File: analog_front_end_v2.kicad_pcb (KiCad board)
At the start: 4 copper layers, 153 parts, among them J1 Conn_Coaxial, J3 Conn_01x01_Socket, J4 Conn_01x01_Socket, U1 ADL5531, U10 PMOD 2x6, U11 LP2985-5.0, U12 LP2985-5.0, U13 LT1363, U14 MAX 735, U15 LP2985-2.5, U16 MAX889SESA, U17 MAX6102, U2 ADL5531, U3 ADL5531, U4 PE4140B-Z, U5 ADF4360-9, U6 LTC1406, U7 THS4551, U8 LT1363, U9 PMOD 2x6

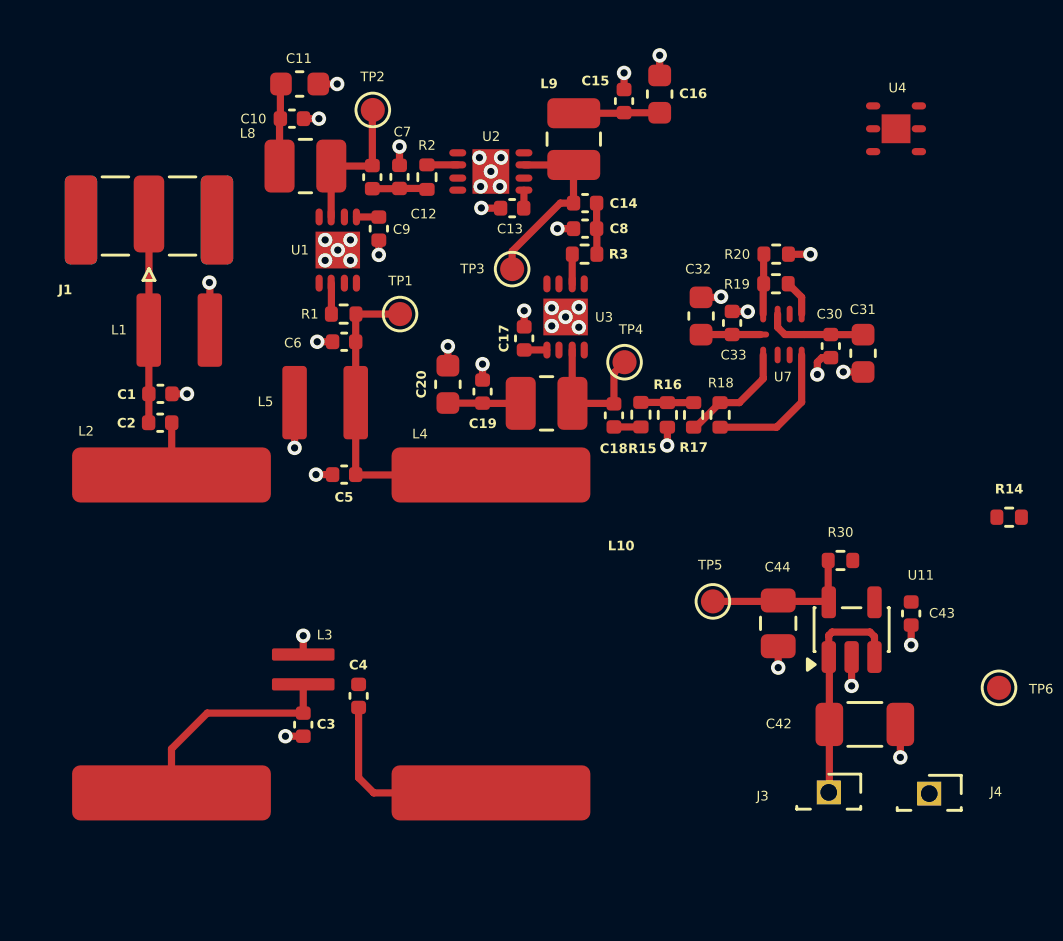
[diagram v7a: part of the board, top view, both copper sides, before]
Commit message: Minor touchups to via placements to bring them as close as possible to the pads for minimized parasitics
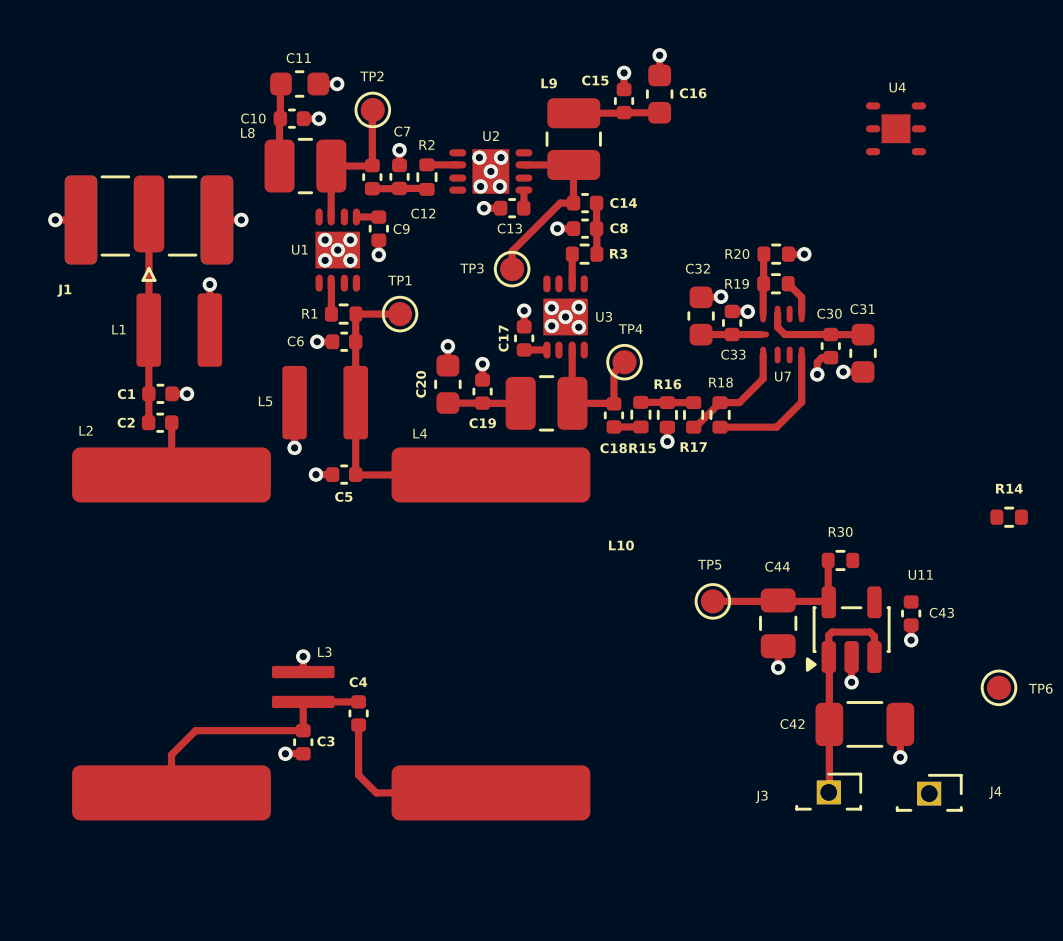
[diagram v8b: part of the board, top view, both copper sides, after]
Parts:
- moved C3 0.73 mm to (23.6, 42.0)
- moved C4 0.73 mm to (25.9, 40.8)
- moved L3 0.73 mm to (23.6, 39.7)
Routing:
- net Net-(C3-Pad1): track 9.12 -> 11.0 mm
- net GND: track 25.9 -> 27.0 mm, vias 44 -> 46
- net Net-(C4-Pad2): track 8.68 -> 7.89 mm
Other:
- board text added: "TODO: Ground via stitching Decisions: Use 0.3mm trace for 50ohm characteristic impedance for microstrip with solid groundplane in layers 2,3 Use 0.4mm silkscreen width/height to balance readability/placement Ensure RF Mixer (U4) is far away from sensitive RF/analog front end"
- board text removed: "TODO: Ground via stitching Decisions: Use 0.3mm trace for 50ohm characteristic impedance for microstrip with solid groundplane Use 0.4mm silkscreen width/height to balance readability/placement Ensure RF Mixer (U4) is far away from sensitive RF/analog front end"
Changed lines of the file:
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@@
 	(footprint "Capacitor_SMD:C_0402_1005Metric"
 		(layer "F.Cu")
-		(at 25.9 40.025 -90)
+		(at 25.9 40.755 -90)
 		(descr "Capacitor SMD 0402 (1005 Metric), square (rectangular) end terminal, IPC-7351 nominal, (Body size source: IPC-SM-782 page 76, https://www.pcb-3d.com/wordpress/wp-content/uploads/ipc-sm-782a_amendment_1_and_2.pdf), generated with kicad-footprint-generator")
 		(tags "capacitor")
@@
 	(footprint "Capacitor_SMD:C_0402_1005Metric"
 		(layer "F.Cu")
-		(at 23.6 41.22 -90)
+		(at 23.6 41.95 -90)
 		(descr "Capacitor SMD 0402 (1005 Metric), square (rectangular) end terminal, IPC-7351 nominal, (Body size source: IPC-SM-782 page 76, https://www.pcb-3d.com/wordpress/wp-content/uploads/ipc-sm-782a_amendment_1_and_2.pdf), generated with kicad-footprint-generator")
 		(tags "capacitor")
@@
 		(tags "capacitor")
 		(property "Reference" "C6"
-			(at 2.13 -0.05 180)
+			(at 2.01 0 180)
 			(layer "F.SilkS")
 			(effects
@@
 		(tags "capacitor")
 		(property "Reference" "C42"
-			(at 3.575 0.025 0)
+			(at 2.995 0 0)
 			(layer "F.SilkS")
 			(effects
@@
 	(footprint "TheEEView_Footprint_Lib:0807SQ-11N"
 		(layer "F.Cu")
-		(at 23.6 38.925 90)
+		(at 23.6 39.655 90)
 		(property "Reference" "L3"
 			(at 1.435 0.89 0)
@@
 		)
 	)
-	(gr_text "TODO: \nGround via stitching\nDecisions:\nUse 0.3mm trace for 50ohm characteristic impedance \nfor microstrip with solid groundplane\nUse 0.4mm silkscreen width/height to balance readability/placement\nEnsure RF Mixer (U4) is far away from sensitive RF/analog front end"
+	(gr_text "TODO: \nGround via stitching\nDecisions:\nUse 0.3mm trace for 50ohm characteristic impedance \nfor microstrip with solid groundplane in layers 2,3\nUse 0.4mm silkscreen width/height to balance readability/placement\nEnsure RF Mixer (U4) is far away from sensitive RF/analog front end"
 		(at 23.59 7.64 0)
 		(layer "Cmts.User")
@@
 	)
 	(segment
+		(start 48.86 37.0825)
+		(end 48.86 37.71)
+		(width 0.3)
+		(layer "F.Cu")
+		(net 2)
+	)
+	(segment
 		(start 25.01 14.6)
 		(end 24.225 14.6)
@@
 	)
 	(segment
-		(start 19.72 22.87)
-		(end 19.7 22.85)
-		(width 0.2)
+		(start 31.05 26.9)
+		(end 31.05 26.24)
+		(width 0.3)
 		(layer "F.Cu")
 		(net 2)
 	)
 	(segment
-		(start 19.72 24.825)
-		(end 19.72 22.87)
+		(start 38.73 29.46)
+		(end 38.73 28.86)
 		(width 0.3)
 		(layer "F.Cu")
@@
 	)
 	(segment
-		(start 31.05 26.9)
-		(end 31.05 26.24)
+		(start 19.72 24.825)
+		(end 19.72 22.93)
 		(width 0.3)
 		(layer "F.Cu")
@@
 	)
 	(segment
-		(start 23.595 41.85)
-		(end 23.6 41.845)
+		(start 23.595 42.58)
+		(end 23.6 42.575)
 		(width 0.2)
 		(layer "F.Cu")
@@
 	)
 	(segment
+		(start 31.8 19.76)
+		(end 31.11 19.76)
+		(width 0.3)
+		(layer "F.Cu")
+		(net 2)
+	)
+	(segment
+		(start 23.6 39.035)
+		(end 23.6 38.39)
+		(width 0.3)
+		(layer "F.Cu")
+		(net 2)
+	)
+	(segment
 		(start 45.52 25.97)
 		(end 45.15 25.97)
@@
 	)
 	(segment
-		(start 23.6 38.305)
-		(end 23.6 37.525)
+		(start 23.6 42.43)
+		(end 22.86 42.43)
 		(width 0.3)
 		(layer "F.Cu")
@@
 	)
 	(segment
-		(start 23.6 41.7)
-		(end 22.86 41.7)
+		(start 43.82 21.675)
+		(end 44.42 21.675)
 		(width 0.3)
 		(layer "F.Cu")
@@
 	)
 	(segment
-		(start 38.73 29.61)
-		(end 38.72 29.62)
-		(width 0.2)
-		(layer "F.Cu")
-		(net 2)
-	)
-	(segment
 		(start 36.93 14.83)
 		(end 36.93 14.14)
@@
 	)
 	(segment
+		(start 27.6 17.98)
+		(end 27.6 17.35)
+		(width 0.3)
+		(layer "F.Cu")
+		(net 2)
+	)
+	(segment
 		(start 34.16 20.61)
 		(end 34.78 20.61)
@@
 	)
 	(segment
+		(start 38.73 29.61)
+		(end 38.73 29.46)
+		(width 0.2)
+		(layer "F.Cu")
+		(net 2)
+	)
+	(segment
 		(start 41.42 24.05)
 		(end 42.06 24.05)
@@
 	)
 	(segment
-		(start 31.8 19.76)
-		(end 31.01 19.76)
+		(start 20.015 20.25)
+		(end 21.03 20.25)
 		(width 0.3)
 		(layer "F.Cu")
@@
 	)
 	(segment
-		(start 46.385 38.41)
-		(end 46.385 39.61)
-		(width 0.3)
-		(layer "F.Cu")
-		(net 2)
-	)
-	(segment
-		(start 31.01 19.76)
-		(end 31 19.75)
-		(width 0.2)
-		(layer "F.Cu")
-		(net 2)
-	)
-	(segment
-		(start 27.6 17.98)
-		(end 27.6 17.2)
+		(start 14.365 20.25)
+		(end 13.3 20.25)
 		(width 0.3)
 		(layer "F.Cu")
@@
 	)
 	(segment
-		(start 48.86 37.0825)
-		(end 48.86 37.91)
+		(start 43.335 37.96)
+		(end 43.335 38.85)
 		(width 0.3)
 		(layer "F.Cu")
@@
 	)
 	(segment
-		(start 43.82 21.675)
-		(end 44.675 21.675)
+		(start 46.385 38.41)
+		(end 46.385 39.46)
 		(width 0.3)
 		(layer "F.Cu")
@@
 	)
 	(segment
-		(start 38.73 28.86)
-		(end 38.73 29.61)
-		(width 0.3)
-		(layer "F.Cu")
-		(net 2)
-	)
-	(segment
-		(start 43.335 37.96)
-		(end 43.335 38.85)
-		(width 0.3)
+		(start 45.925 26.565)
+		(end 46.04 26.565)
+		(width 0.2)
 		(layer "F.Cu")
 		(net 2)
 	)
 	(segment
-		(start 45.925 26.565)
-		(end 46.04 26.565)
+		(start 31.01 19.76)
+		(end 31.11 19.76)
 		(width 0.2)
 		(layer "F.Cu")
@@
 	)
 	(via
-		(at 31 19.75)
+		(at 31.11 19.76)
 		(size 0.6)
 		(drill 0.3)
@@
 	)
 	(via
-		(at 44.675 21.675)
+		(at 44.42 21.675)
 		(size 0.6)
 		(drill 0.3)
@@
 	)
 	(via
-		(at 46.385 39.61)
+		(at 46.385 39.46)
 		(size 0.6)
 		(drill 0.3)
@@
 	)
 	(via
-		(at 38.72 29.62)
+		(at 38.73 29.46)
 		(size 0.6)
 		(drill 0.3)
@@
 	)
 	(via
-		(at 48.86 37.91)
+		(at 48.86 37.71)
 		(size 0.6)
 		(drill 0.3)
@@
 	)
 	(via
-		(at 27.6 17.2)
+		(at 27.6 17.35)
 		(size 0.6)
 		(drill 0.3)
@@
 	)
 	(via
-		(at 22.86 41.7)
+		(at 13.3 20.25)
+		(size 0.6)
+		(drill 0.3)
+		(layers "F.Cu" "B.Cu")
+		(free yes)
+		(net 2)
+	)
+	(via
+		(at 22.86 42.43)
 		(size 0.6)
 		(drill 0.3)
@@
 	)
 	(via
-		(at 19.7 22.85)
+		(at 19.72 22.93)
 		(size 0.6)
 		(drill 0.3)
@@
 	)
 	(via
+		(at 21.03 20.25)
+		(size 0.6)
+		(drill 0.3)
+		(layers "F.Cu" "B.Cu")
+		(free yes)
+		(net 2)
+	)
+	(via
 		(at 34.16 20.61)
 		(size 0.6)
@@
 	)
 	(via
-		(at 23.6 37.525)
+		(at 23.6 38.39)
 		(size 0.6)
 		(drill 0.3)
@@
 	)
 	(segment
-		(start 18.125 42.225)
-		(end 18.125 44.055)
+		(start 19.13 41.47)
+		(end 23.6 41.47)
+		(width 0.3)
+		(layer "F.Cu")
+		(net 4)
+	)
+	(segment
+		(start 25.9 40.275)
+		(end 23.6 40.275)
 		(width 0.3)
 		(layer "F.Cu")
@@
 	)
 	(segment
-		(start 19.61 40.74)
-		(end 18.125 42.225)
+		(start 23.6 41.47)
+		(end 23.6 40.275)
 		(width 0.3)
 		(layer "F.Cu")
@@
 	)
 	(segment
-		(start 23.6 40.74)
-		(end 23.6 39.545)
+		(start 18.125 42.475)
+		(end 19.13 41.47)
 		(width 0.3)
 		(layer "F.Cu")
@@
 	)
 	(segment
-		(start 23.6 40.74)
-		(end 19.61 40.74)
+		(start 18.125 44.055)
+		(end 18.125 42.475)
 		(width 0.3)
 		(layer "F.Cu")
@@
 	)
 	(segment
-		(start 26.53 44.055)
-		(end 31.4 44.055)
+		(start 26.635 44.055)
+		(end 25.9 43.32)
 		(width 0.3)
 		(layer "F.Cu")
@@
 	)
 	(segment
-		(start 25.9 43.425)
-		(end 26.53 44.055)
+		(start 31.4 44.055)
+		(end 26.635 44.055)
 		(width 0.3)
 		(layer "F.Cu")
@@
 	)
 	(segment
-		(start 25.9 40.505)
-		(end 25.9 43.425)
+		(start 25.9 43.32)
+		(end 25.9 41.235)
 		(width 0.3)
 		(layer "F.Cu")
